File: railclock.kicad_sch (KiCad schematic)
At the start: 177 parts, among them J1 Conn_01x02_Pin, J10 Conn_01x04_MountingPin, J11 Conn_01x04_MountingPin, J12 Conn_01x04_MountingPin, J13 Conn_01x04_MountingPin, J14 Conn_01x04_MountingPin, J15 Conn_01x03_MountingPin, J16 Barrel_Jack_Switch, J2 Conn_01x03_MountingPin, J3 Conn_01x04_MountingPin, J4 USB_C_Receptacle_USB2.0_14P, J5 Conn_01x03_MountingPin, J6 Conn_01x03_MountingPin, J7 Conn_01x03_MountingPin, J8 Conn_01x03_MountingPin, J9 Conn_01x04_MountingPin, Q1 Q_NPN_BEC, SW1 SW_SPST, SW2 SW_DPDT_x2, U1 MCP7940N-xST, U10 74AHC1G04, U11 MAX811TEUS-T, U12 MCP4728, U13 BTS5012SDA, U14 BTS5012SDA, U15 BTS5012SDA, U16 BTS5012SDA, U17 BTS5012SDA, U2 MCP73832-2-OT, U4 ESP32-C6-WROOM-1, U5 DRV8870DDA, U6 PAM2421, U8 BQ24296MRGET, U9 PCF8574RGTR, Y1 MC-306_32.7680K-A5__ROHS

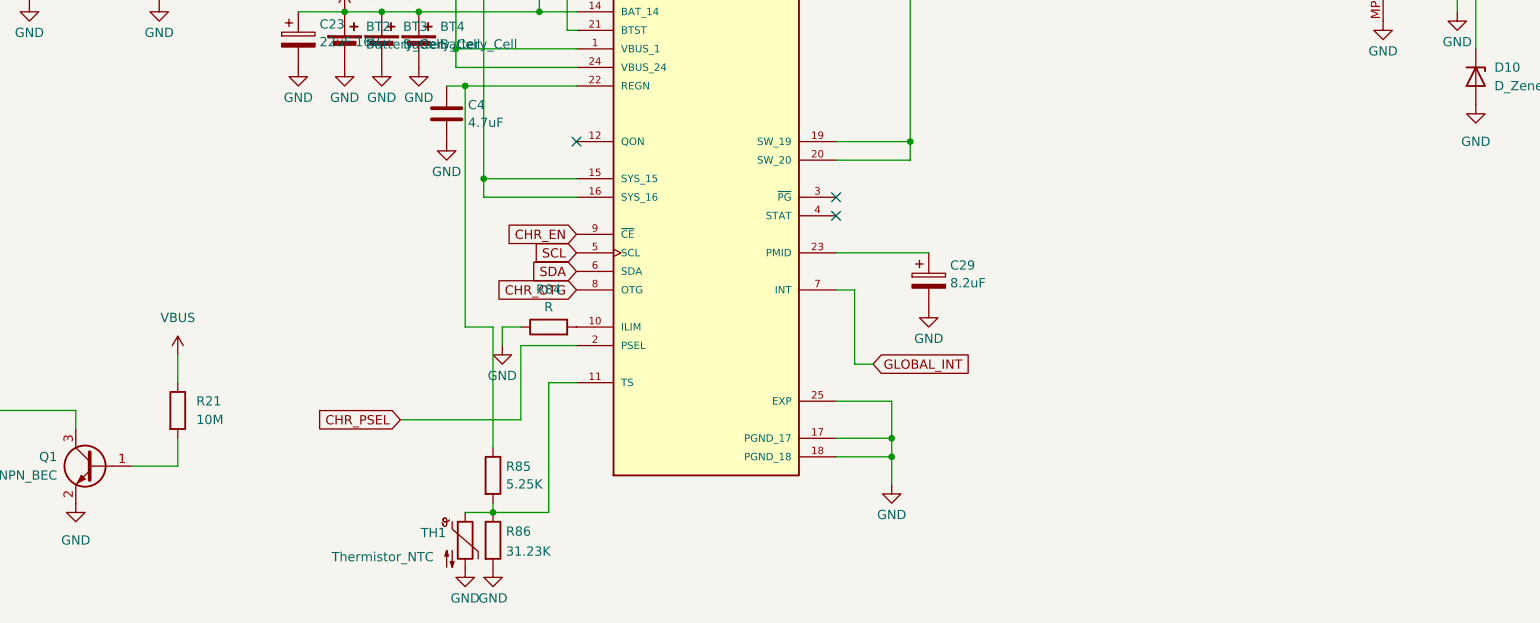
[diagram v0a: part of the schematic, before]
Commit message: Fix VBUS detection and add wakeup button
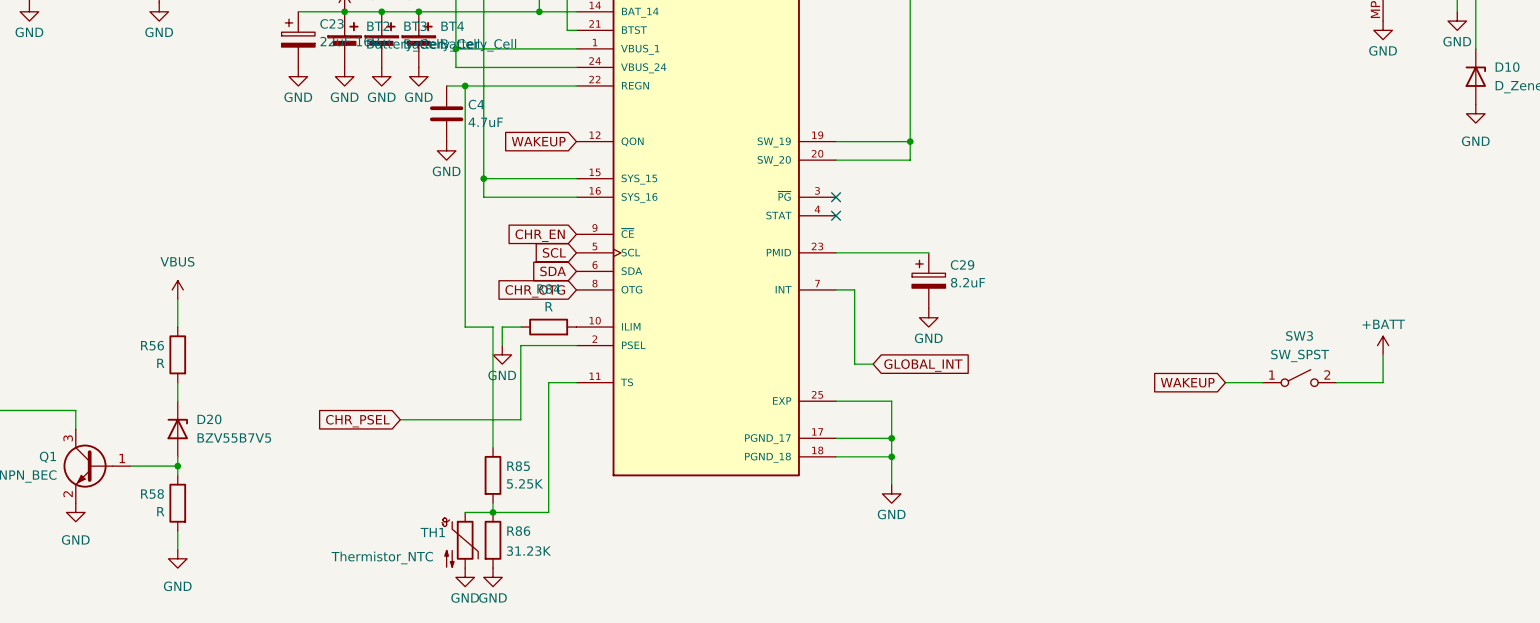
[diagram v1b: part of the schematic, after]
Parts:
- removed R21: 10M, Resistor_SMD:R_0805_2012Metric, symbol Device:R
- added D20: BZV55B7V5, Diode_SMD:D_MiniMELF, symbol Diode:BZV55B7V5
- added R56, R58: R, Resistor_SMD:R_0805_2012Metric, symbol Device:R
- added SW3: SW_SPST, Button_Switch_SMD:Panasonic_EVQPUL_EVQPUC, symbol Switch:SW_SPST
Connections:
- net +BATT: now also SW3.2 (B)
- net GND: now also R58.2
- net IN: now also R56.1
- net WAKEUP: now reaches U8.12 (QON)
- net WAKEUP: now also SW3.1 (A)
- net at Q1.1 (B): now also D20.2 (A), R58.1
- new net: D20.1 (K), R56.2
- no-connect marks 4 -> 3
